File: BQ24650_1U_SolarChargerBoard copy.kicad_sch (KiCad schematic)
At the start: 49 parts, among them J1 Solar IO, J2 Battery IO, J3 CE_MPPSET, Q1 Q_NMOS_GDS, Q2 Q_NMOS_GDS, Q3 Q_NMOS_GDS, U1 BQ24650

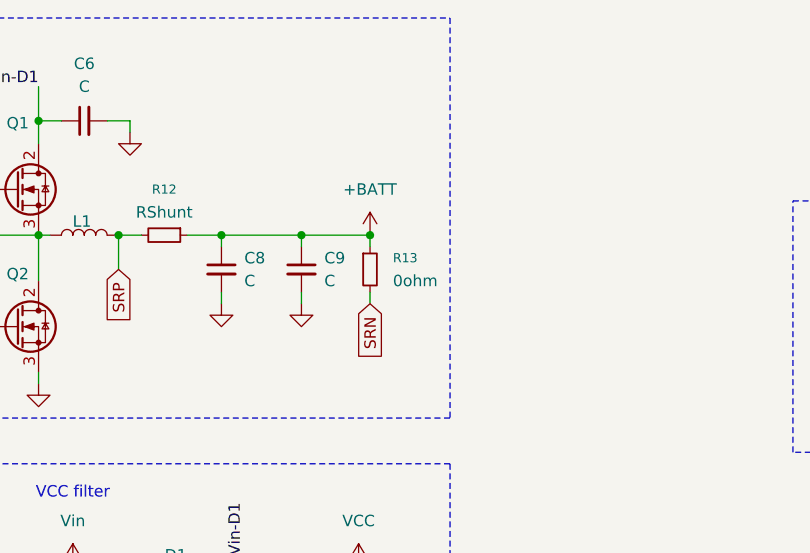
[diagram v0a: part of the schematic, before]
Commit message: Assigned footprints
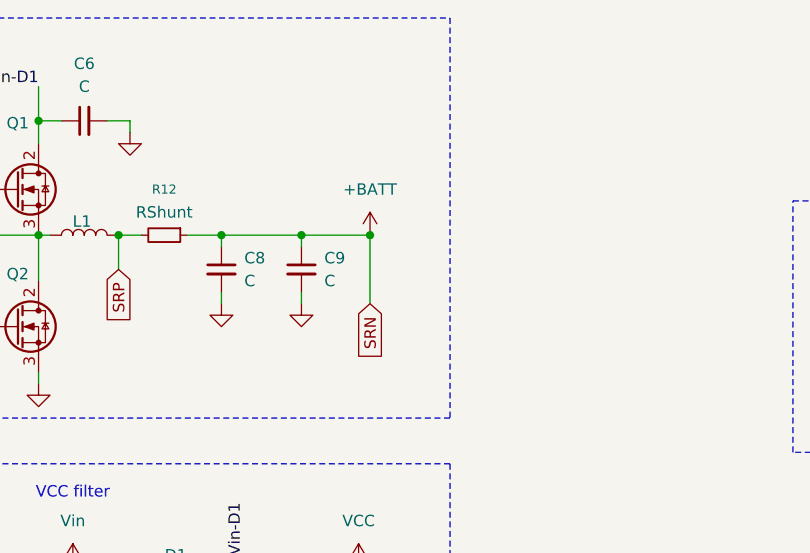
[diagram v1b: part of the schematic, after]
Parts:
- removed R13: 0ohm, symbol Device:R_Small
- C1, C6, C8, C9: footprint (none) -> Capacitor_SMD:C_1210_3225Metric
- C10, D3, D4: footprint (none) -> Capacitor_SMD:C_0603_1608Metric
- C2, C3, C4, C5, C7: footprint (none) -> Capacitor_SMD:C_0805_2012Metric
- D1: footprint (none) -> Diode_SMD:D_PowerDI-5
- D2, Q3: footprint (none) -> Package_TO_SOT_SMD:SOT-23
- J1: footprint (none) -> Connector_PinHeader_2.54mm:PinHeader_1x02_P2.54mm_Vertical
- J2: footprint (none) -> Connector_PinHeader_2.54mm:PinHeader_1x03_P2.54mm_Vertical
- J3: footprint (none) -> Connector_PinHeader_2.54mm:PinHeader_1x01_P2.54mm_Vertical
- L1: footprint (none) -> Inductor_SMD:L_Vishay_IHLP-2525
- Q1, Q2: footprint (none) -> Package_SO:PowerPAK_SO-8_Dual
- R1, R10, R11, R2, R3, R4, R7, R8, R9: footprint (none) -> Resistor_SMD:R_0402_1005Metric
- R12, R6: footprint (none) -> Resistor_SMD:R_1206_3216Metric
- R5: footprint (none) -> Resistor_SMD:R_2512_6332Metric
- RV1, RV2: footprint (none) -> Potentiometer_THT:Potentiometer_Bourns_3296W_Vertical
- TP1, TP10, TP11, TP12, TP2, TP3, TP4, TP5, TP6, TP7, TP8, TP9: footprint (none) -> TestPoint:TestPoint_Pad_D1.5mm
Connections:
- net SRN is gone; now on net +BATT: C7.2, U1.9 (SRN)
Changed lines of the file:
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@@
 	(wire
 		(pts
-			(xy 147.32 57.15) (xy 147.32 55.88)
-		)
-		(stroke
-			(width 0)
-			(type default)
-		)
-	)
-	(wire
-		(pts
 			(xy 146.05 100.33) (xy 146.05 99.06)
 		)
@@
 	(wire
 		(pts
+			(xy 147.32 49.53) (xy 147.32 57.15)
+		)
+		(stroke
+			(width 0)
+			(type default)
+		)
+	)
+	(wire
+		(pts
 			(xy 143.51 165.1) (xy 148.59 165.1)
 		)
@@
 	(wire
 		(pts
-			(xy 147.32 50.8) (xy 147.32 49.53)
-		)
-		(stroke
-			(width 0)
-			(type default)
-		)
-	)
-	(wire
-		(pts
 			(xy 46.99 90.17) (xy 46.99 91.44)
 		)
@@
 			)
 		)
-		(property "Footprint" ""
+		(property "Footprint" "Capacitor_SMD:C_1210_3225Metric"
 			(at 139.7 53.34 0)
 			(hide yes)
@@
 			)
 		)
-		(property "Footprint" ""
+		(property "Footprint" "Connector_PinHeader_2.54mm:PinHeader_1x02_P2.54mm_Vertical"
 			(at 209.55 125.73 0)
 			(hide yes)
@@
 			)
 		)
-		(property "Footprint" ""
+		(property "Footprint" "Capacitor_SMD:C_0603_1608Metric"
 			(at 130.81 165.1 0)
 			(hide yes)
@@
 			)
 		)
-		(property "Footprint" ""
+		(property "Footprint" "Resistor_SMD:R_0402_1005Metric"
 			(at 140.97 154.94 0)
 			(hide yes)
@@
 			)
 		)
-		(property "Footprint" ""
+		(property "Footprint" "Resistor_SMD:R_0402_1005Metric"
 			(at 52.07 60.96 0)
 			(hide yes)
@@
 			)
 		)
-		(property "Footprint" ""
+		(property "Footprint" "Capacitor_SMD:C_1210_3225Metric"
 			(at 130.81 53.34 0)
 			(hide yes)
@@
 			)
 		)
-		(property "Footprint" ""
+		(property "Footprint" "Capacitor_SMD:C_0805_2012Metric"
 			(at 146.05 96.52 0)
 			(hide yes)
@@
 			)
 		)
-		(property "Footprint" ""
+		(property "Footprint" "Inductor_SMD:L_Vishay_IHLP-2525"
 			(at 115.57 49.53 0)
 			(hide yes)
@@
 			)
 		)
-		(property "Footprint" ""
+		(property "Footprint" "TestPoint:TestPoint_Pad_D1.5mm"
 			(at 52.07 62.23 0)
 			(hide yes)
@@
 			)
 		)
-		(property "Footprint" ""
+		(property "Footprint" "Potentiometer_THT:Potentiometer_Bourns_3296W_Vertical"
 			(at 82.55 163.83 0)
 			(hide yes)
@@
 			)
 		)
-		(property "Footprint" ""
+		(property "Footprint" "Diode_SMD:D_PowerDI-5"
 			(at 125.73 91.44 0)
 			(hide yes)
@@
 			)
 		)
-		(property "Footprint" ""
+		(property "Footprint" "Resistor_SMD:R_0402_1005Metric"
 			(at 55.88 40.64 0)
 			(hide yes)
@@
 			)
 		)
-		(property "Footprint" ""
+		(property "Footprint" "Connector_PinHeader_2.54mm:PinHeader_1x03_P2.54mm_Vertical"
 			(at 224.79 127 0)
 			(hide yes)
@@
 			)
 		)
-		(property "Footprint" ""
+		(property "Footprint" "TestPoint:TestPoint_Pad_D1.5mm"
 			(at 205.74 60.96 0)
 			(hide yes)
@@
 			)
 		)
-		(property "Footprint" ""
+		(property "Footprint" "TestPoint:TestPoint_Pad_D1.5mm"
 			(at 218.44 60.96 0)
 			(hide yes)
@@
 			)
 		)
-		(property "Footprint" ""
+		(property "Footprint" "Resistor_SMD:R_2512_6332Metric"
 			(at 114.3 95.25 0)
 			(hide yes)
@@
 			)
 		)
-		(property "Footprint" ""
+		(property "Footprint" "Capacitor_SMD:C_0603_1608Metric"
 			(at 90.17 151.13 0)
 			(hide yes)
@@
 			)
 		)
-		(property "Footprint" ""
+		(property "Footprint" "Resistor_SMD:R_1206_3216Metric"
 			(at 139.7 91.44 0)
 			(hide yes)
@@
 			)
 		)
-		(property "Footprint" ""
+		(property "Footprint" "Capacitor_SMD:C_0805_2012Metric"
 			(at 78.74 106.68 0)
 			(hide yes)
@@
 			)
 		)
-		(property "Footprint" ""
+		(property "Footprint" "TestPoint:TestPoint_Pad_D1.5mm"
 			(at 210.82 62.23 0)
 			(hide yes)
@@
 			)
 		)
-		(property "Footprint" ""
+		(property "Footprint" "Package_SO:PowerPAK_SO-8_Dual"
 			(at 113.03 41.91 0)
 			(hide yes)
@@
 			)
 		)
-		(property "Footprint" ""
+		(property "Footprint" "Capacitor_SMD:C_0805_2012Metric"
 			(at 100.33 52.07 0)
 			(hide yes)
@@
 			)
 		)
-		(property "Footprint" ""
+		(property "Footprint" "Resistor_SMD:R_0402_1005Metric"
 			(at 45.72 163.83 0)
 			(hide yes)
@@
 			)
 		)
-		(property "Footprint" ""
+		(property "Footprint" "Package_TO_SOT_SMD:SOT-23"
 			(at 129.54 125.73 0)
 			(hide yes)
@@
 			)
 		)
-		(property "Footprint" ""
+		(property "Footprint" "Package_SO:PowerPAK_SO-8_Dual"
 			(at 113.03 57.15 0)
 			(hide yes)
@@
 			)
 		)
-		(property "Footprint" ""
+		(property "Footprint" "Capacitor_SMD:C_0805_2012Metric"
 			(at 137.16 121.92 0)
 			(hide yes)
@@
 			)
 		)
-		(property "Footprint" ""
+		(property "Footprint" "Capacitor_SMD:C_1210_3225Metric"
 			(at 114.3 100.33 0)
 			(hide yes)
@@
 			)
 		)
-		(property "Footprint" ""
+		(property "Footprint" "Potentiometer_THT:Potentiometer_Bourns_3296W_Vertical"
 			(at 55.88 53.34 0)
 			(hide yes)
@@
 			)
 		)
-		(property "Footprint" ""
+		(property "Footprint" "TestPoint:TestPoint_Pad_D1.5mm"
 			(at 215.9 60.96 0)
 			(hide yes)
@@
 			)
 		)
-		(property "Footprint" ""
+		(property "Footprint" "TestPoint:TestPoint_Pad_D1.5mm"
 			(at 78.74 160.02 0)
 			(hide yes)
@@
 			)
 		)
-		(property "Footprint" ""
+		(property "Footprint" "Capacitor_SMD:C_0805_2012Metric"
 			(at 46.99 93.98 0)
 			(hide yes)
@@
 			)
 		)
-		(property "Footprint" ""
+		(property "Footprint" "Connector_PinHeader_2.54mm:PinHeader_1x01_P2.54mm_Vertical"
 			(at 195.58 125.73 0)
 			(hide yes)
@@
 			)
 		)
-		(property "Footprint" ""
+		(property "Footprint" "TestPoint:TestPoint_Pad_D1.5mm"
 			(at 208.28 60.96 0)
 			(hide yes)
@@
 			)
 		)
-		(property "Footprint" ""
+		(property "Footprint" "Resistor_SMD:R_0402_1005Metric"
 			(at 78.74 168.91 0)
 			(hide yes)
@@
 			)
 		)
-		(property "Footprint" ""
+		(property "Footprint" "Capacitor_SMD:C_0603_1608Metric"
 			(at 130.81 154.94 0)
 			(hide yes)
@@
 			)
 		)
-		(property "Footprint" ""
+		(property "Footprint" "Capacitor_SMD:C_1210_3225Metric"
 			(at 115.57 36.83 0)
 			(hide yes)
@@
 			)
 		)
-		(property "Footprint" ""
+		(property "Footprint" "TestPoint:TestPoint_Pad_D1.5mm"
 			(at 223.52 60.96 0)
 			(hide yes)
@@
 			)
 		)
-		(property "Footprint" ""
+		(property "Footprint" "Package_TO_SOT_SMD:SOT-23"
 			(at 48.26 48.26 0)
 			(hide yes)
@@
 	)
 	(symbol
-		(lib_id "Device:R_Small")
-		(at 147.32 53.34 0)
-		(unit 1)
-		(body_style 1)
-		(exclude_from_sim no)
-		(in_bom yes)
-		(on_board yes)
-		(in_pos_files yes)
-		(dnp no)
-		(fields_autoplaced yes)
-		(property "Reference" "R13"
-			(at 149.86 52.0699 0)
-			(show_name no)
-			(do_not_autoplace no)
-			(effects
-				(font
-					(size 1.016 1.016)
-				)
-				(justify left)
-			)
-		)
-		(property "Value" "0ohm"
-			(at 149.86 54.6099 0)
-			(show_name no)
-			(do_not_autoplace no)
-			(effects
-				(font
-					(size 1.27 1.27)
-				)
-				(justify left)
-			)
-		)
-		(property "Footprint" ""
-			(at 147.32 53.34 0)
-			(hide yes)
-			(show_name no)
-			(do_not_autoplace no)
-			(effects
-				(font
-					(size 1.27 1.27)
-				)
-			)
-		)
-		(property "Datasheet" ""
-			(at 147.32 53.34 0)
-			(hide yes)
-			(show_name no)
-			(do_not_autoplace no)
-			(effects
-				(font
-					(size 1.27 1.27)
-				)
-			)
-		)
-		(property "Description" "Resistor, small symbol"
-			(at 147.32 53.34 0)
-			(hide yes)
-			(show_name no)
-			(do_not_autoplace no)
-			(effects
-				(font
-					(size 1.27 1.27)
-				)
-			)
-		)
-		(pin "1"
-		)
-		(pin "2"
-		)
-		(instances
-			(project "BQ24650_1U_SolarChargerBoard"
-				(path "/97f2ae87-13ff-4eec-a108-f469a6765d40"
-					(reference "R13")
-					(unit 1)
-				)
-			)
-		)
-	)
-	(symbol
 		(lib_id "Connector:TestPoint")
 		(at 215.9 60.96 180)
@@
 			)
 		)
-		(property "Footprint" ""
+		(property "Footprint" "TestPoint:TestPoint_Pad_D1.5mm"
 			(at 210.82 60.96 0)
 			(hide yes)
@@
 			)
 		)
-		(property "Footprint" ""
+		(property "Footprint" "Resistor_SMD:R_0402_1005Metric"
 			(at 82.55 152.4 0)
 			(hide yes)
@@
 			)
 		)
-		(property "Footprint" ""
+		(property "Footprint" "Resistor_SMD:R_0402_1005Metric"
 			(at 45.72 156.21 0)
 			(hide yes)
@@
 			)
 		)
-		(property "Footprint" ""
+		(property "Footprint" "TestPoint:TestPoint_Pad_D1.5mm"
 			(at 203.2 60.96 0)
 			(hide yes)
@@
 			)
 		)
-		(property "Footprint" ""
+		(property "Footprint" "Resistor_SMD:R_1206_3216Metric"
 			(at 124.46 49.53 0)
 			(hide yes)
@@
 			)
 		)
-		(property "Footprint" ""
+		(property "Footprint" "Resistor_SMD:R_0402_1005Metric"
 			(at 36.83 99.06 0)
 			(hide yes)
@@
 			)
 		)
-		(property "Footprint" ""
+		(property "Footprint" "Resistor_SMD:R_0402_1005Metric"
 			(at 140.97 165.1 0)
 			(hide yes)
@@
 			)
 		)
-		(property "Footprint" ""
+		(property "Footprint" "TestPoint:TestPoint_Pad_D1.5mm"
 			(at 213.36 60.96 0)
 			(hide yes)
@@
 			)
 		)
-		(property "Footprint" ""
+		(property "Footprint" "TestPoint:TestPoint_Pad_D1.5mm"
 			(at 220.98 60.96 0)
 			(hide yes)

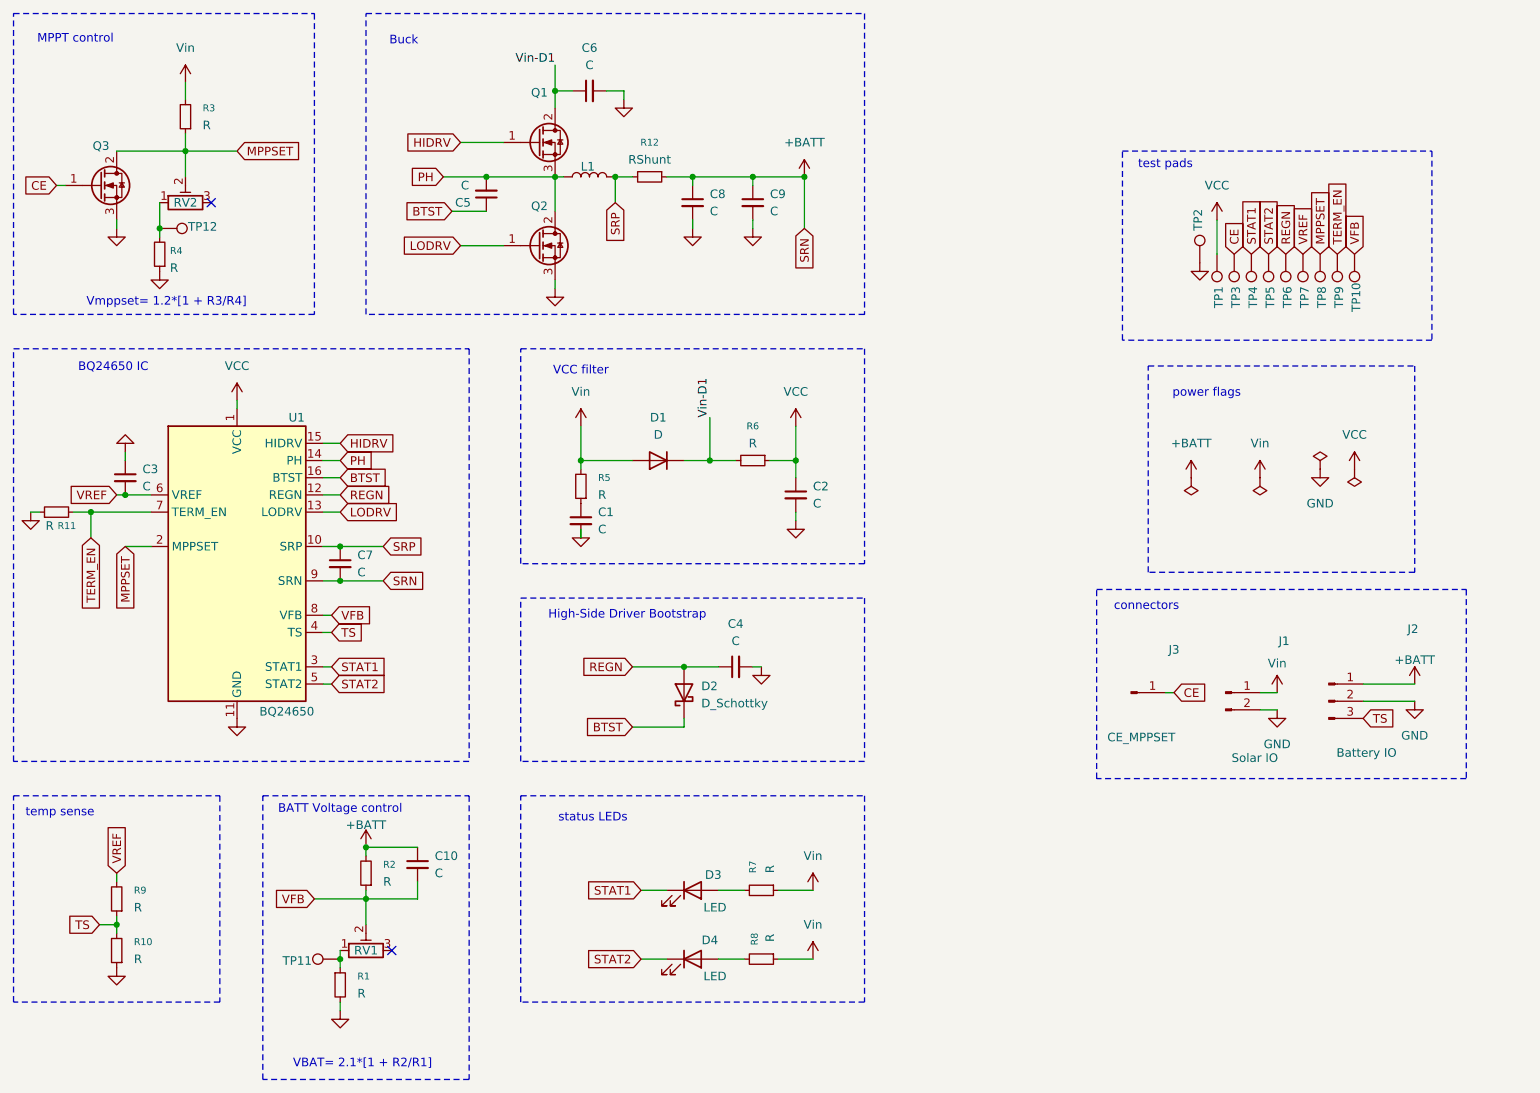
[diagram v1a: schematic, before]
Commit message: decided Front and back components
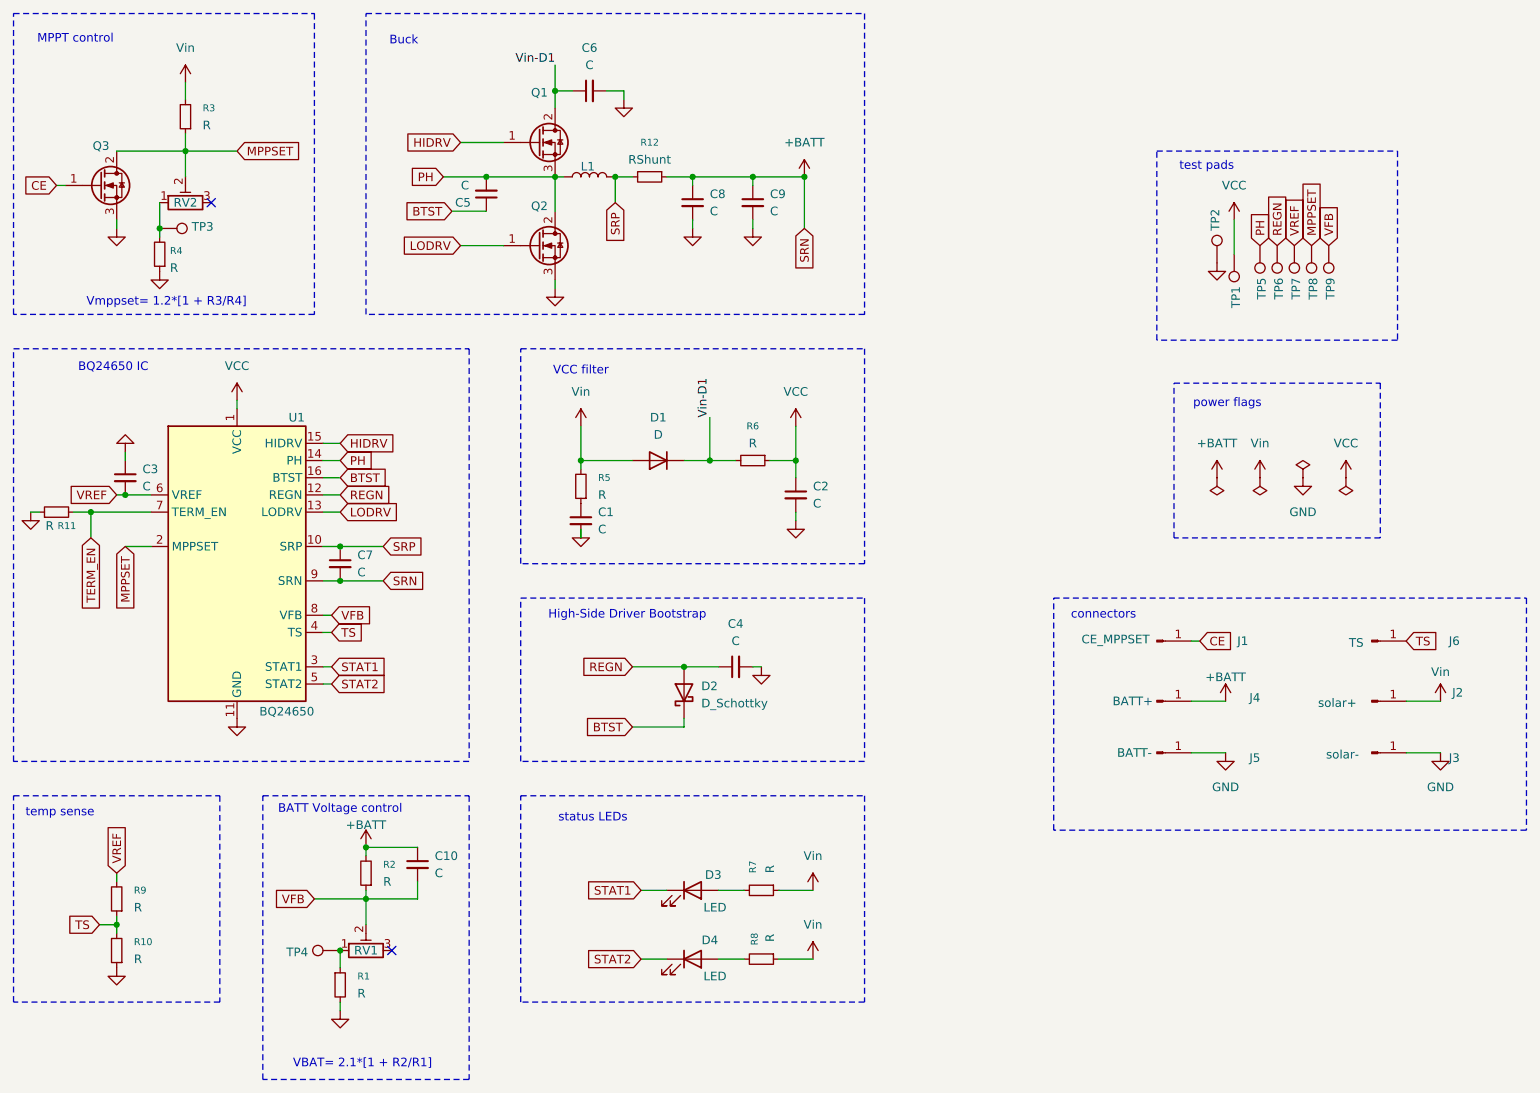
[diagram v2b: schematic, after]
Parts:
- removed J1: Solar IO, Connector_PinHeader_2.54mm:PinHeader_1x02_P2.54mm_Vertical, symbol Connector:Conn_01x02_Pin
- removed J2: Battery IO, Connector_PinHeader_2.54mm:PinHeader_1x03_P2.54mm_Vertical, symbol Connector:Conn_01x03_Pin
- removed TP10, TP11, TP12: TestPoint, TestPoint:TestPoint_Pad_D1.5mm, symbol Connector:TestPoint
- added J2: solar+, Connector_PinHeader_2.54mm:PinHeader_1x01_P2.54mm_Vertical, symbol Connector:Conn_01x01_Pin
- added J3: solar-, Connector_PinHeader_2.54mm:PinHeader_1x01_P2.54mm_Vertical, symbol Connector:Conn_01x01_Pin
- added J4: BATT+, Connector_PinHeader_2.54mm:PinHeader_1x01_P2.54mm_Vertical, symbol Connector:Conn_01x01_Pin
- added J5: BATT-, Connector_PinHeader_2.54mm:PinHeader_1x01_P2.54mm_Vertical, symbol Connector:Conn_01x01_Pin
- added J6: TS, Connector_PinHeader_2.54mm:PinHeader_1x01_P2.54mm_Vertical, symbol Connector:Conn_01x01_Pin
- C1, C6, C8, C9: footprint Capacitor_SMD:C_1210_3225Metric -> Capacitor_SMD:C_0805_2012Metric
- R12: footprint Resistor_SMD:R_1206_3216Metric -> Resistor_SMD:R_2512_6332Metric
- renumbered J3 to J1
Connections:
- net +BATT: now also J4.1 (Pin_1)
- net CE: no longer TP3.1
- net GND: now also J3.1 (Pin_1), J5.1 (Pin_1)
- net PH: now also TP5.1
- net STAT1: no longer TP4.1
- net STAT2: no longer TP5.1
- net TERM_EN: no longer TP9.1
- net TS: now also J6.1 (Pin_1)
- net VFB: now also TP9.1
- net Vin: now also J2.1 (Pin_1)
- net at R4.2, RV2.1: now also TP3.1
- net at R1.1, RV1.1: now also TP4.1
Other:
- moved on the sheet: J1, TP1, TP2
